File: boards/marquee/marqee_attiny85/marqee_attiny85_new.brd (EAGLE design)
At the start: 37.9 x 24 mm, 11 parts, among them U1 ATTINY85-20PU

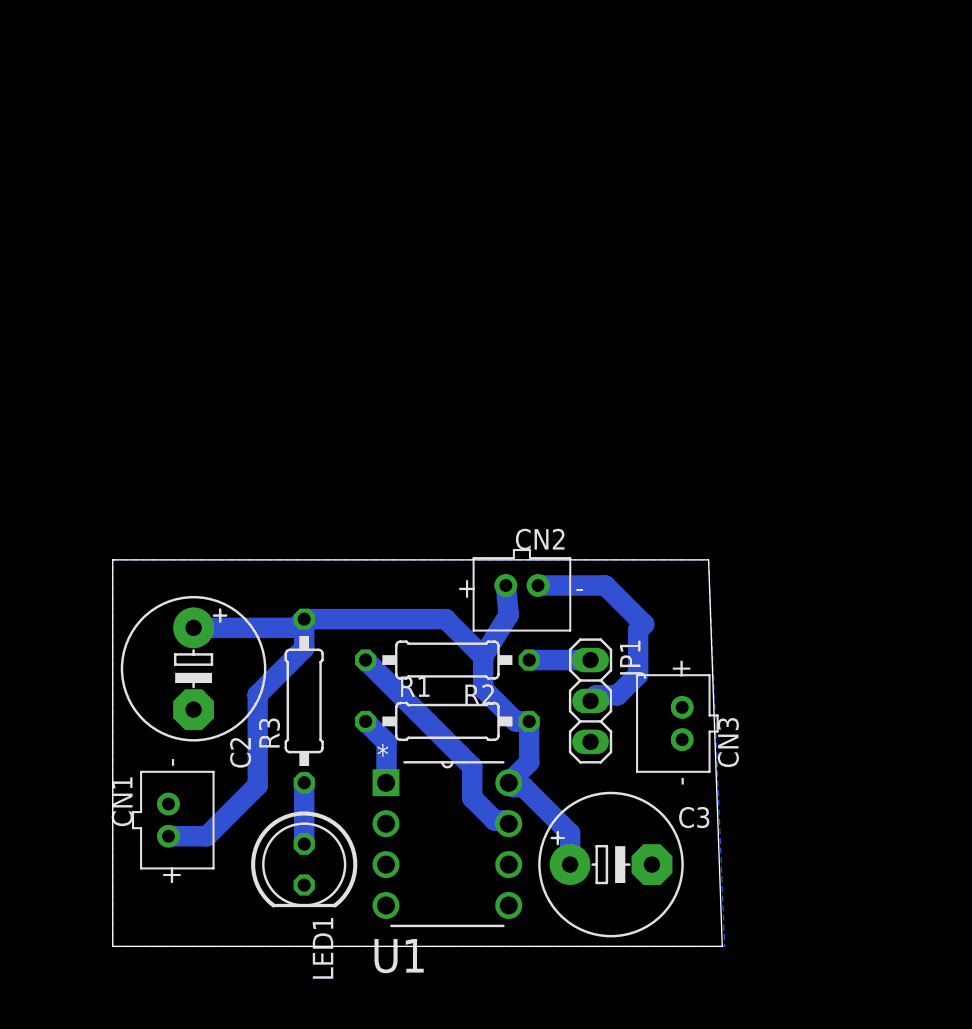
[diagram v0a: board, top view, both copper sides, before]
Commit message: class 3 materials; adds Arrow-NeoPixel PCB
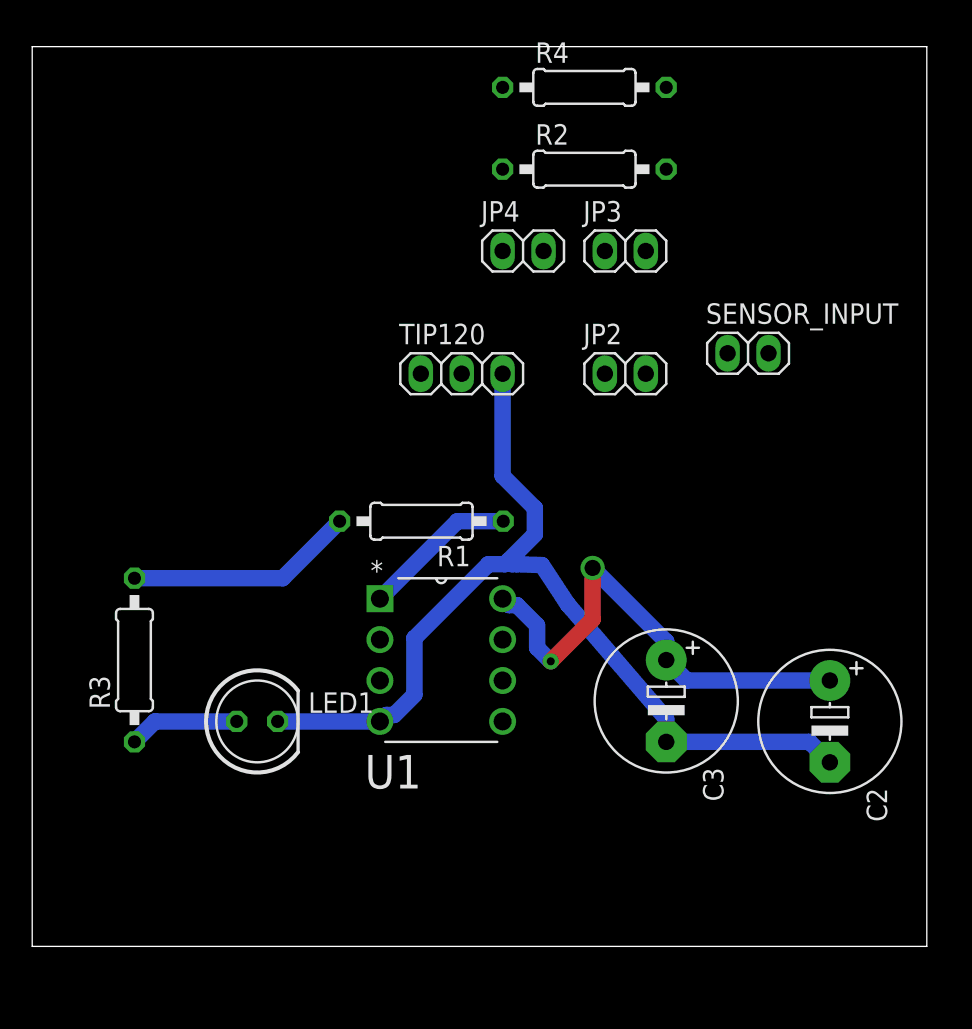
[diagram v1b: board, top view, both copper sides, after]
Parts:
- removed CN1, CN2, CN3: (no value), adafruit-2014:JST-PH-2-THM
- removed JP1: (no value), pinhead:1X03
- added JP2, JP3, JP4, SENSOR_INPUT: (no value), pinhead:1X02
- added R4: 1k, resistor:0207/10
- added TIP120: (no value), pinhead:1X03
- C2, C3: value (none) -> 47uF
- R1: value (none) -> 10k
- R2: value (none) -> 1k
- R3: value (none) -> 220
- moved C2 39.6 mm to (49.5, 14.0)
- moved R2 31.6 mm to (34.3, 48.3), turned to 0 degrees
- moved R1 12.5 mm to (24.2, 26.4), turned to 180 degrees
- moved U1 11.4 mm to (29.2, 14.0)
- moved R3 10.8 mm to (6.35, 17.8)
- moved C3 10.7 mm to (39.4, 15.2), turned to 270 degrees
- moved LED1 9.36 mm to (14.0, 14.0), turned to 0 degrees
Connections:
- removed net N$6: CN2.2, JP1.2
- new net ANALOG_SENSOR_IN: R4.1, SENSOR_INPUT.1, U1.7
- new net THING: JP2.1, TIP120.2
- net GND: now also JP3.1, JP4.1, R4.2, TIP120.3; no longer CN1.2, CN3.2, JP1.3
- net N$2: now also TIP120.1; no longer JP1.1
- net N$4: now also U1.5; no longer U1.7
- net VCC: now also JP2.2, JP3.2, JP4.2, SENSOR_INPUT.2; no longer CN1.1, CN2.1, CN3.1
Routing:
- net GND: track 0.00 -> 60.2 mm
- net VCC: track 59.5 -> 44.8 mm, vias 0 -> 2
- net N$6: track 14.5 -> 0.00 mm
- net N$4: track 14.2 -> 0.00 mm
- net N$1: track 4.55 -> 9.65 mm
- net N$2: track 3.81 -> 0.00 mm
- net N$3: track 3.81 -> 6.88 mm
- removed copper zone on layer 16, net GND
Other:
- board size 37.9 x 24 mm -> 55.5 x 55.9 mm
